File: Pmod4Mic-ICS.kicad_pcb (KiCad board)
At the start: 2 copper layers, 25.4 x 99.1 mm, 6 parts, among them J1 CONN_01X06

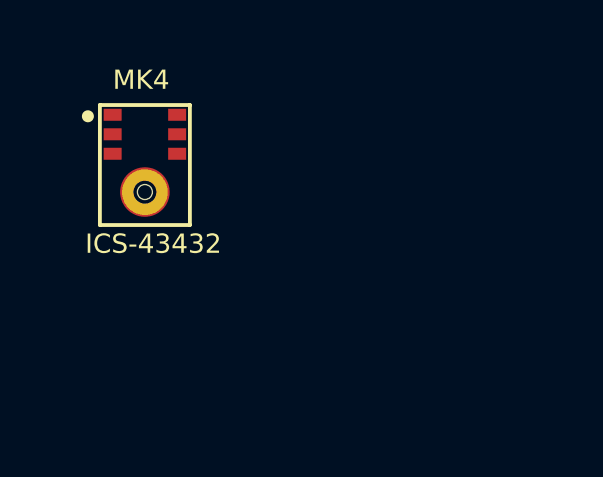
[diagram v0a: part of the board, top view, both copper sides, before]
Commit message: Added line labels and fixed errors
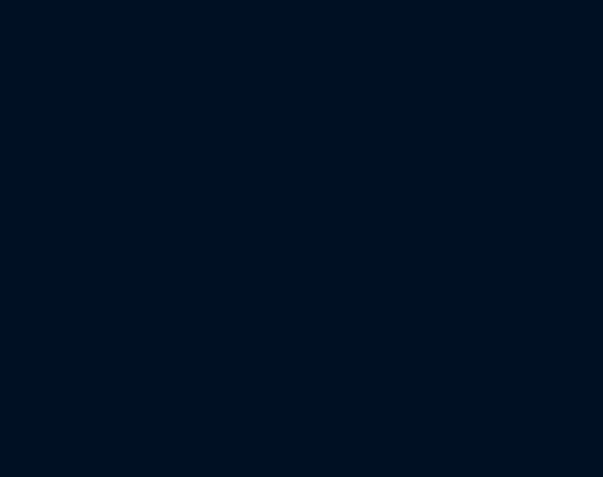
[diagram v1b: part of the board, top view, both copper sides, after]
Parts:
- removed the MK4 at (0.00, 0.00)
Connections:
- net Net-(J1-Pad1) renamed /D1
- net Net-(J1-Pad2) renamed /D0
- net Net-(J1-Pad3) renamed /SCLK
- net Net-(J1-Pad5) renamed /GND
- net Net-(J1-Pad6) renamed /VDD
- J1 pad 4: Net-(J1-Pad4) -> /WS/WCLK
- MK1 pad 5: Net-(J1-Pad4) -> /WS/WCLK
- MK2 pad 5: Net-(J1-Pad4) -> /WS/WCLK
- MK3 pad 5: (no net) -> /WS/WCLK
- MK4 pad 5: Net-(J1-Pad4) -> /WS/WCLK
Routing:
- net Net-(J1-Pad4): track 105.5 -> 0.00 mm, vias 4 -> 0
- net /WS/WCLK: track 0.00 -> 105.5 mm, vias 0 -> 4
- net /VDD: track 118.7 -> 122.5 mm
- net /GND: track 140.6 -> 136.9 mm

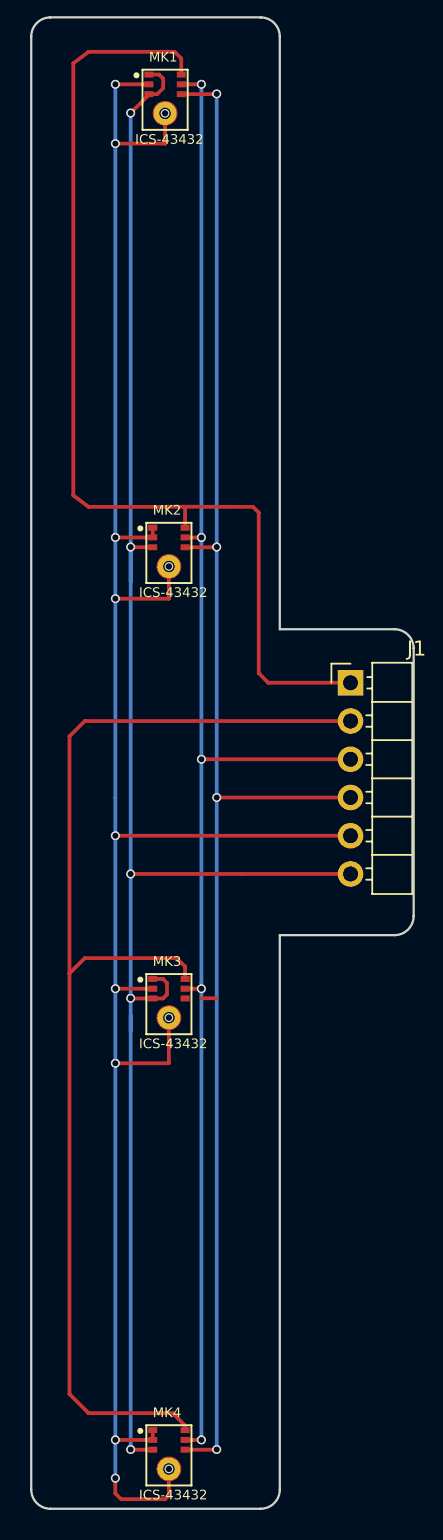
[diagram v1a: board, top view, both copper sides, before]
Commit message: Adding test points, caps, and Resistors with passing ERC/DRC
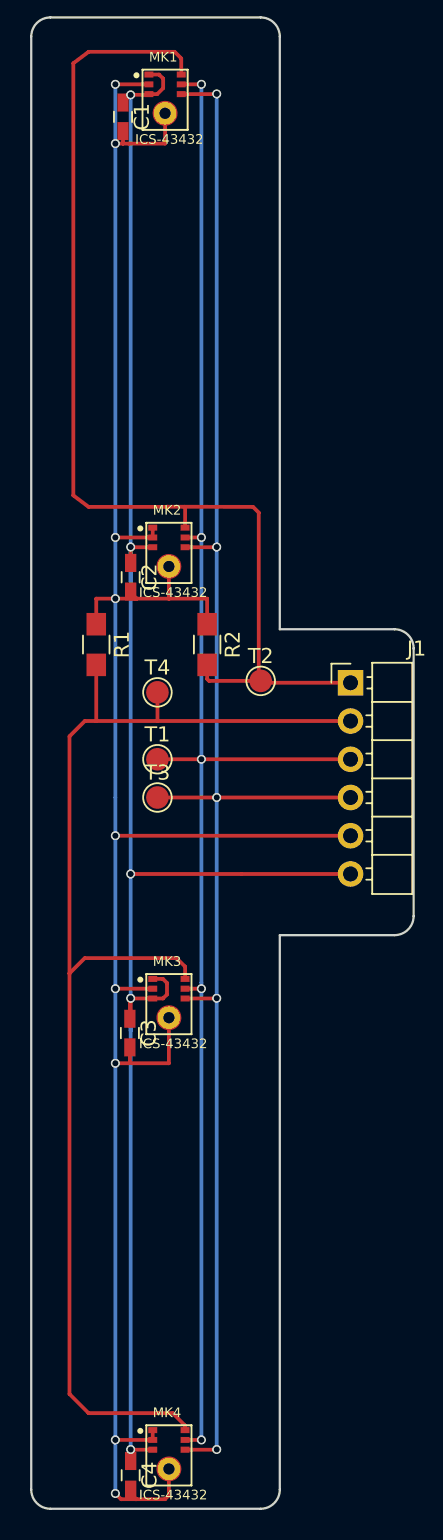
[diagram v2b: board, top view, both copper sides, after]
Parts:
- added C1: 0.1uF, Capacitors_SMD:C_0603_HandSoldering, F.Cu at (109.4, 23.0)
- added C2: 0.1uF, Capacitors_SMD:C_0603_HandSoldering, F.Cu at (109.9, 53.6)
- added C3: 0.1uF, Capacitors_SMD:C_0603_HandSoldering, F.Cu at (109.9, 83.8)
- added C4: 0.1uF, Capacitors_SMD:C_0603_HandSoldering, F.Cu at (109.9, 113.2)
- added R1: 100k, Resistors_SMD:R_0805_HandSoldering, F.Cu at (107.6, 58.0)
- added R2: 100k, Resistors_SMD:R_0805_HandSoldering, F.Cu at (115.0, 58.0)
- added T1: TEST_1P, TestPoint:TestPoint_Pad_D1.5mm, F.Cu at (111.7, 65.6)
- added T2: TEST_1P, TestPoint:TestPoint_Pad_D1.5mm, F.Cu at (118.5, 60.4)
- added T3: TEST_1P, TestPoint:TestPoint_Pad_D1.5mm, F.Cu at (111.7, 68.2)
- added T4: TEST_1P, TestPoint:TestPoint_Pad_D1.5mm, F.Cu at (111.7, 61.2)
- J1: value CONN_01X06 -> PMOD_01x06
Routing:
- net /GND: track 136.9 -> 152.9 mm
- net /WS/WCLK: track 105.5 -> 111.6 mm, vias 4 -> 5
- net /D0: track 80.8 -> 86.4 mm
- net /D1: track 68.6 -> 73.2 mm
- net /SCLK: track 104.6 -> 107.5 mm
- net /VDD: track 122.5 -> 124.8 mm
- net (no net): track 1.02 -> 0.00 mm
